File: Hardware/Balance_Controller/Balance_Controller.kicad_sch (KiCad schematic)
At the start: 101 parts, among them J1 COM_SW, J10 VESC-, J11 SWD, J12 BLE PROG, J13 RGB_LED, J14 ENABLE, J15 CAN, J2 CHRG_SW, J3 LOAD_SW, J4 BATT+, J5 BATT-, J6 BAL_BATT, J7 BAL_CHRG, J8 CHARGE, J9 VESC+, SW1 NRST, SW2 BOOT0, T1 TestPoint, T10 TestPoint, T11 TestPoint, T2 TestPoint, T3 TestPoint, T4 TestPoint, T6 TestPoint, T7 TestPoint, U1 MPM3610GQV-P, U2 MPM3610GQV-P, U3 TPS2116DRLR, U4 MCP111T-195I/LB, U5 STM32F412CGU6, U6 RN4871-I/RM140, U7 TJA1051TK-3, U8 MPU-6050, Y1 NX3225SA-16.000

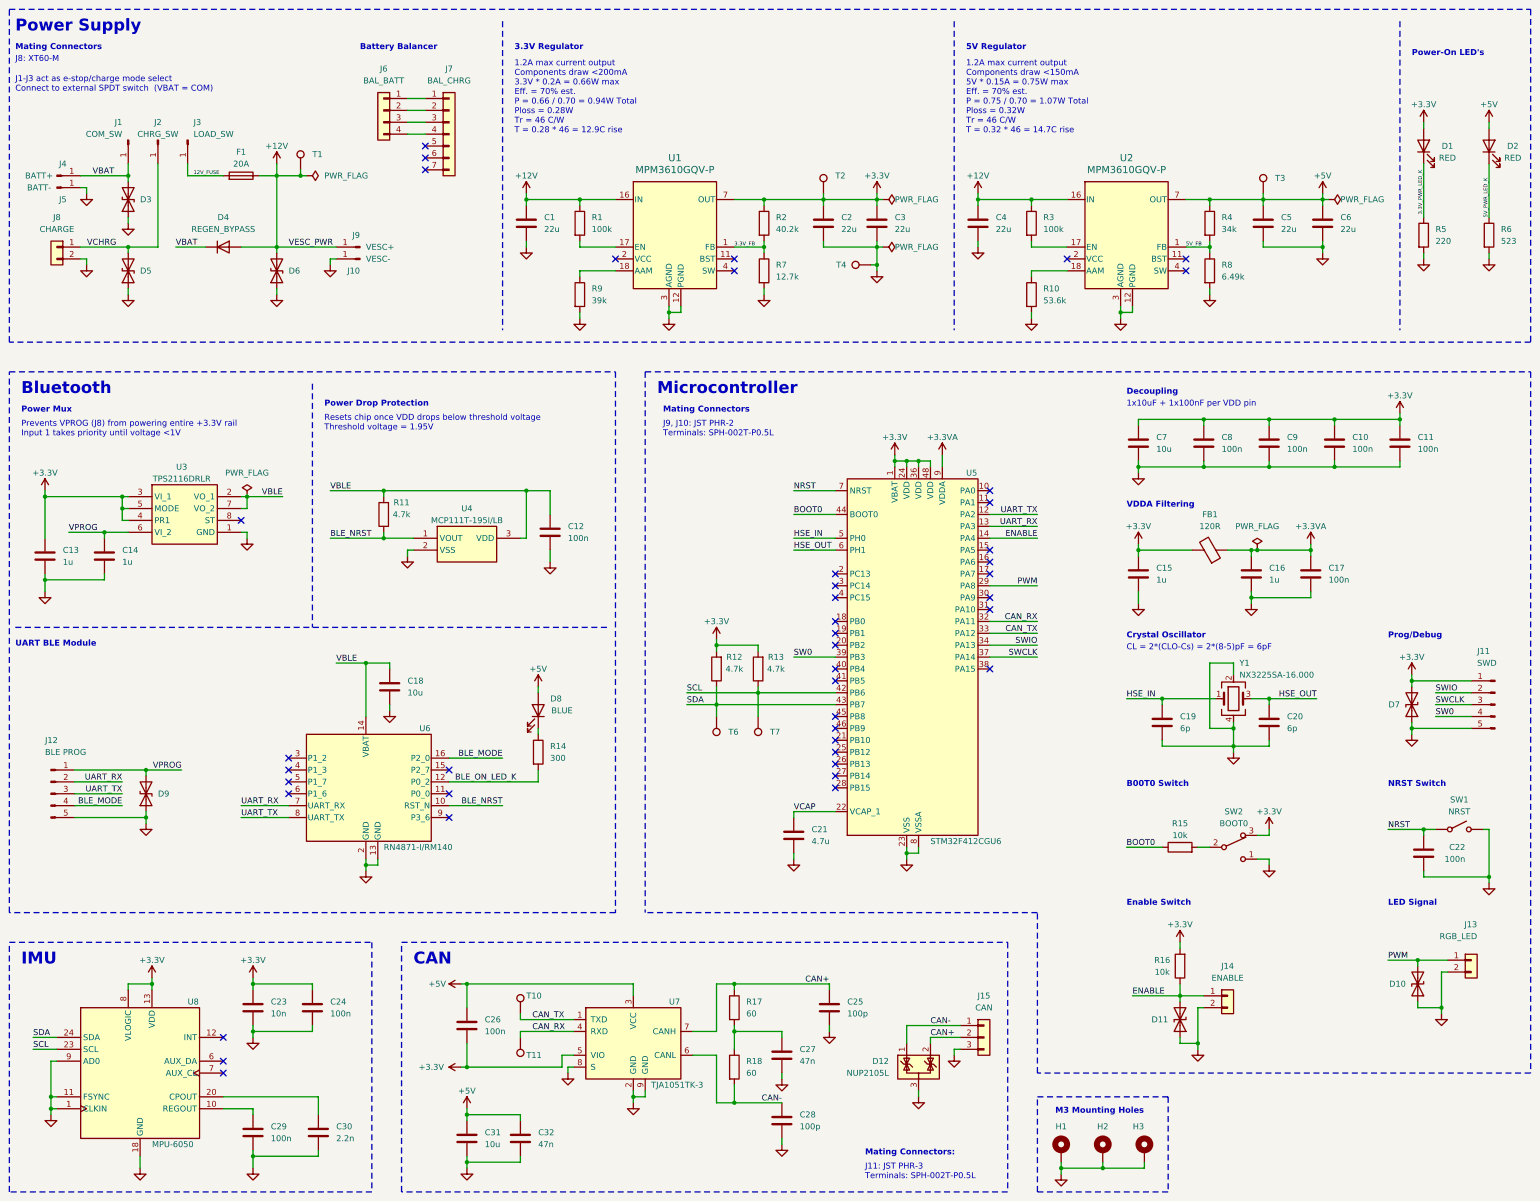
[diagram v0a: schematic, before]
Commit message: Updated schematic and routing
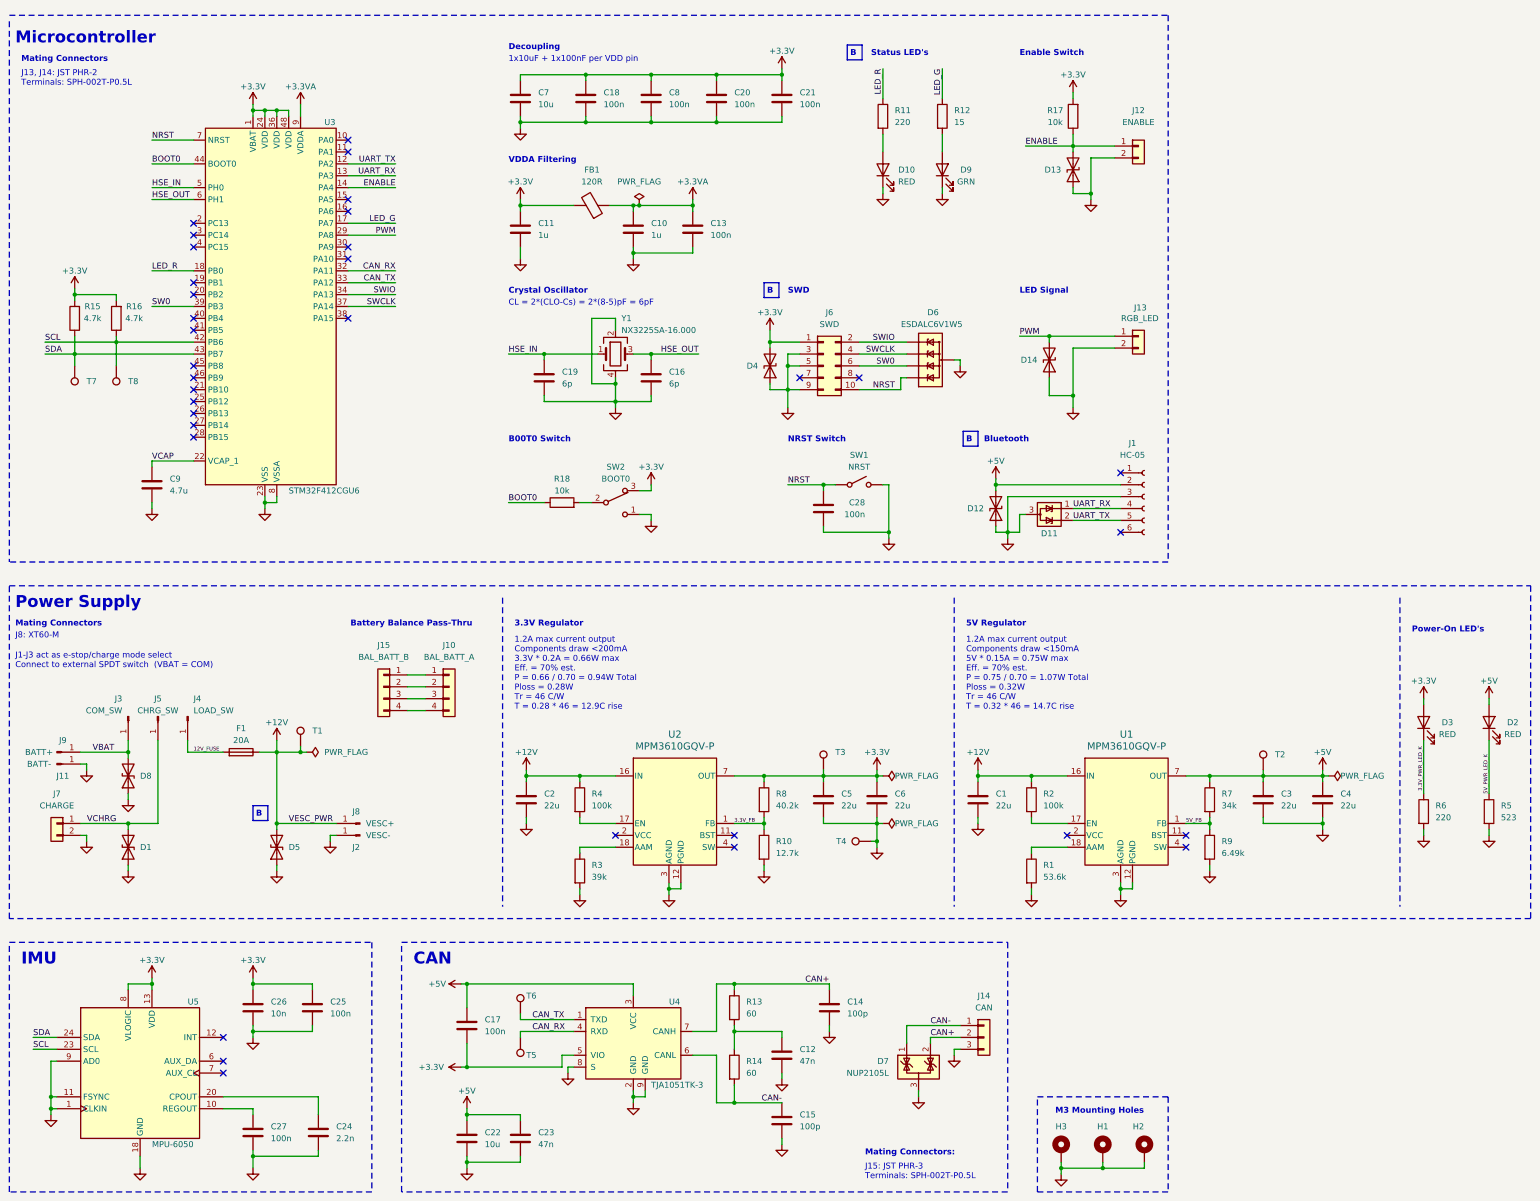
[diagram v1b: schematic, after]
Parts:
- removed C12: 100n, Capacitor_SMD:C_0603_1608Metric, symbol Device:C
- removed C13, C14: 1u, Capacitor_SMD:C_0805_2012Metric, symbol Device:C
- removed C18: 10u, Capacitor_SMD:C_1206_3216Metric, symbol Device:C
- removed D4: REGEN_BYPASS, SBM3060VDC-AU_R2_006A1:SBM3060VDCAU_R2_006A1, symbol SBM3060VDC-AU_R2_006A1:SBM3060VDC-AU_R2_006A1
- removed D7, D9: SC1533-01FTG, Diode_SMD:D_SOD-323, symbol Device:D_TVS
- removed D8: BLUE, LED_SMD:LED_0805_2012Metric, symbol Device:LED
- removed J11: SWD, Connector_PinHeader_1.27mm:PinHeader_1x05_P1.27mm_Vertical, symbol Connector:Conn_01x05_Pin
- removed J12: BLE PROG, Connector_PinHeader_1.27mm:PinHeader_1x05_P1.27mm_Vertical, symbol Connector:Conn_01x05_Pin
- removed J7: BAL_CHRG, Connector_JST:JST_XH_B7B-XH-A_1x07_P2.50mm_Vertical, symbol Connector_Generic:Conn_01x07
- removed R14: 300, Resistor_SMD:R_0603_1608Metric, symbol Device:R
- removed U3: TPS2116DRLR, TPS2116DRLR:SOTFL50P160X60-8N, symbol TPS2116DRLR:TPS2116DRLR
- removed U4: MCP111T-195I/LB, MCP111T-195I/LB:SOT65P210X110-3N, symbol MCP111T-195I_LB:MCP111T-195I_LB
- removed U6: RN4871-I/RM140, RN4871-I/RM140:RN4871_MCH, symbol RN4871-I/RM140:RN4871-I_RM140
- added D10: RED, LED_SMD:LED_0805_2012Metric, symbol Device:LED
- added D11: VESD03A2-03G-G3-08, Package_TO_SOT_SMD:SOT-323_SC-70, symbol VESD: VESD03A2-03G-G3-08
- added D12, D4: SC1533-01FTG, Diode_SMD:D_SOD-323, symbol Device:D_TVS
- added D6: ESDALC6V1W5, ESDALC6V1W5:SOT65P210X110-5N, symbol ESDALC6V1W5:ESDALC6V1W5
- added D9: GRN, LED_SMD:LED_0805_2012Metric, symbol Device:LED
- added J1: HC-05, Connector_PinSocket_2.54mm:PinSocket_1x06_P2.54mm_Vertical, symbol Connector:Conn_01x06_Socket
- added J10: BAL_BATT_A, Connector_JST:JST_XH_B4B-XH-A_1x04_P2.50mm_Vertical, symbol Connector_Generic:Conn_01x04
- added J6: SWD, Connector_PinHeader_1.27mm:PinHeader_2x05_P1.27mm_Vertical_SMD, symbol Connector_Generic:Conn_02x05_Odd_Even
- added R12: 15, Resistor_SMD:R_0603_1608Metric, symbol Device:R
- J15: renamed from J6; value BAL_BATT -> BAL_BATT_B
- R11: value 4.7k -> 220; PN MCT0603MD4701BP500 -> ERJ-UP3J221V
- T1: footprint RCU-0C:TP+195X110 -> RCT-0C:RCT-0C; MPN RCU-0C -> RCT-0C
- T2: renamed from T3; footprint RCU-0C:TP+195X110 -> RCT-0C:RCT-0C; PN RCU-0C -> RCT-0C
- T3: renamed from T2; footprint RCU-0C:TP+195X110 -> RCT-0C:RCT-0C; PN RCU-0C -> RCT-0C
- T4: footprint RCU-0C:TP+195X110 -> RCT-0C:RCT-0C
- U3: renamed from U5; footprint Package_DFN_QFN:QFN-48-1EP_7x7mm_P0.5mm_EP5.6x5.6mm -> STM32F412:QFN-48-1EP_7x7mm_P0.5mm_EP5.6x5.6mm
- U5: renamed from U8; footprint Sensor_Motion:InvenSense_QFN-24_4x4mm_P0.5mm -> MPU6050:InvenSense_QFN-24_4x4mm_P0.5mm
- renumbered C4 to C1, C16 to C10, C15 to C11, C27 to C12, C17 to C13, C25 to C14, C28 to C15, C20 to C16, C26 to C17, C8 to C18, C1 to C2, C10 to C20, C11 to C21, C31 to C22, C32 to C23, C30 to C24, C24 to C25, C23 to C26, C29 to C27, C22 to C28, C5 to C3, C6 to C4, C2 to C5, C3 to C6, C9 to C8, C21 to C9, D5 to D1, D11 to D13, D10 to D14, D1 to D3, D6 to D5, D12 to D7, D3 to D8, H2 to H1, H3 to H2, H1 to H3, J5 to J11, J14 to J12, J15 to J14, J10 to J2, J1 to J3, J3 to J4, J2 to J5, J8 to J7, J9 to J8, J4 to J9, R10 to R1, R7 to R10, R17 to R13, R18 to R14, R12 to R15, R13 to R16, R16 to R17, R15 to R18, R3 to R2, R9 to R3, R1 to R4, R6 to R5, R5 to R6, R4 to R7, R2 to R8, R8 to R9, T11 to T5, T10 to T6, T6 to T7, T7 to T8, U2 to U1, U1 to U2, U7 to U4
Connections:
- net BLE_NRST is gone; now on net LED_R: R11.1
- net +3.3V: now also D4.2 (A2), J6.1 (Pin_1)
- net +5V: now also D12.2 (A2), J1.2 (Pin_2)
- net GND: now also D10.1 (K), D11.3 (GND), D12.1 (A1), D4.1 (A1), D6.2 (GND), D9.1 (K), J1.3 (Pin_3), J6.3 (Pin_3), J6.5 (Pin_5), J6.9 (Pin_9)
- net NRST: now also D6.1 (IO1), J6.10 (Pin_10)
- net SW0: now also D6.5 (IO4), J6.6 (Pin_6)
- net SWCLK: now also D6.4 (IO3), J6.4 (Pin_4)
- net SWIO: now also D6.3 (IO2), J6.2 (Pin_2)
- net UART_RX: now also D11.1 (IO1), J1.4 (Pin_4)
- net UART_TX: now also D11.2 (IO2), J1.5 (Pin_5)
- net LED_G: now reaches U3.17 (PA7)
- net LED_G: now also R12.1
- net LED_R: now reaches U3.18 (PB0)
- net at J15.1 (Pin_1): now also J10.1 (Pin_1)
- net at J15.2 (Pin_2): now also J10.2 (Pin_2)
- net at J15.3 (Pin_3): now also J10.3 (Pin_3)
- net at J15.4 (Pin_4): now also J10.4 (Pin_4)
- net VBLE: no longer names the net of R11.2
- net VBLE: now also D10.2 (A)
- new net: D9.2 (A), R12.2
- no-connect marks 43 -> 34
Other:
- note added: "B"
- note added: "Battery Balance Pass-Thru"
- note added: "J13, J14: JST PHR-2 Terminals: SPH-002T-P0.5L"
- note added: "J15: JST PHR-3 Terminals: SPH-002T-P0.5L"
- note added: "SWD"
- note added: "Status LED's"
- note removed: "Battery Balancer"
- note removed: "J11: JST PHR-3 Terminals: SPH-002T-P0.5L"
- note removed: "J9, J10: JST PHR-2 Terminals: SPH-002T-P0.5L"
- note removed: "Power Drop Protection"
- note removed: "Power Mux"
- note removed: "Prevents VPROG (J8) from powering entire +3.3V rail Input 1 takes priority until voltage <1V"
- note removed: "Prog/Debug"
- note removed: "Resets chip once VDD drops below threshold voltage Threshold voltage = 1.95V"
- note removed: "UART BLE Module"
- company: Created By: Austyn Loehr -> (none)
- title: Reaction Wheel Controller -> Balance Controller
- moved on the sheet: C1, C10, C11, C13, C16, C18, C19, C2, C20, C21, C28, C3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

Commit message: Created updated BOM and manufacturing files
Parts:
- C1, C2, C3, C4, C5, C6: MFG (none) -> Murata; MPN (none) -> GRM32ER71E226KE15L; PN GRM32ER71E226KE15L -> (none)
- C10, C11: MFG (none) -> Murata; MPN (none) -> GRM21BR71C105KA01K; PN GRM21BR71C105KA01K -> (none)
- C12, C23: MFG (none) -> Murata; MPN (none) -> GCJ188R71C473KA01D; PN GCJ188R71C473KA01D -> (none)
- C13, C17, C18, C20, C21, C25, C27, C28, C8: MFG (none) -> Murata; MPN (none) -> GRM188R72A104KA35J; PN GRM188R72A104KA35J -> (none)
- C14, C15: MFG (none) -> Murata; MPN (none) -> GCM1885C1H101JA16J; PN GCM1885C1H101JA16J -> (none)
- C16, C19: MFG (none) -> Murata; MPN (none) -> GRM1885C2A6R0DA01D; PN GRM1885C2A6R0DA01D -> (none)
- C22, C7: MFG (none) -> Murata; MPN (none) -> GRM31CR71E106MA12L; PN GRM31CR71E106MA12L -> (none)
- C24: MFG (none) -> Murata; MPN (none) -> GRT1885C1H222JA02D; PN GRT1885C1H222JA02D -> (none)
- C26: MFG (none) -> Murata; MPN (none) -> GRM1885C1H103JA01J; PN GRM1885C1H103JA01J -> (none)
- C9: MFG (none) -> Murata; MPN (none) -> GRM21BZ71E475KE15L; PN GRM21BZ71E475KE15L -> (none)
- D1, D5: MFG (none) -> Panjit; Manufacturer Panjit -> (none)
- D10, D2, D3: MFG (none) -> Wurth Elektronik; MPN (none) -> 150080SS75000; PN 150080SS75000 -> (none)
- D11: MFG (none) -> Vishay; MPN (none) -> VESD03A2-03G-G3-08; Manufacturer_Part_Number 78-VESD03A2-03G-G308 -> (none); Mouser Part Number VESD03A2-03G-G3-08 -> (none)
- D12, D13, D14, D4: MFG (none) -> Littelfuse; MPN (none) -> SC1533-01FTG; PN SC1533-01FTG -> (none)
- D6: MFG (none) -> ST; MPN (none) -> ESDALC6V1W5; Manufacturer_Name STMicroelectronics -> (none); Manufacturer_Part_Number ESDALC6V1W5 -> (none)
- D7: MFG (none) -> Diotec; MPN (none) -> NUP2105L
- D8: MFG (none) -> Panjit; Manufactuer Panjit -> (none)
- D9: MFG (none) -> Wurth Elektronik; Manufacturer Wurth Elektronik -> (none)
- F1: MFG (none) -> Keystone Electronics; Manufacturer_Name Keystone Electronics -> (none); Manufacturer_Part_Number 3568 -> (none)
- FB1: MFG (none) -> Murata; MPN (none) -> BLM18KG121TN1D; PN BLM18KG121TN1D -> (none)
- H1, H2, H3, J11, J2, J3, J4, J5, J8, J9: now left out of the parts list
- J1: MFG (none) -> Wurth Elektronik; MPN (none) -> 61300611821
- J10, J15: MFG (none) -> JST; Manufacturer JST -> (none)
- J12, J13: MFG (none) -> JST; MPN (none) -> B2B-PH-K; PN B2B-PH-K -> (none)
- J14: MFG (none) -> JST; MPN (none) -> B3B-PH-K; PN B3B-PH-K -> (none)
- J6: MFG (none) -> Samtec; Manufacturer Samtec -> (none)
- J7: MFG (none) -> AMASS; Manufacturer AMASS -> (none)
- R1: MFG (none) -> Panasonic; MPN (none) -> ERJ-PA3F5362V; PN ERJ-PA3F5362V -> (none)
- R10: MFG (none) -> Vishay; MPN (none) -> CRCW060312K7FKEAHP; PN CRCW060312K7FKEAHP -> (none)
- R11, R6: MFG (none) -> Panasonic; MPN (none) -> ERJ-UP3J221V; PN ERJ-UP3J221V -> (none)
- R12: MFG (none) -> Panasonic; MPN (none) -> ERJ-UP3F15R0V; Manufacturer Panasonic -> (none); PN ERJ-UP3F15R0V -> (none)
- R13, R14: MFG (none) -> Panasonic; MPN (none) -> ERJ-UP3F60R4V; PN ERJ-UP3F60R4V -> (none)
- R15, R16: MFG (none) -> Vishay; MPN (none) -> MCT0603MD4701BP500; PN MCT0603MD4701BP500 -> (none)
- R17, R18: MFG (none) -> ROHM; MPN (none) -> ESR03EZPJ103; PN ESR03EZPJ103 -> (none)
- R2, R4: MFG (none) -> Panasonic; MPN (none) -> ERJ-UP3F1003V; PN ERJ-UP3F1003V -> (none)
- R3: MFG (none) -> Panasonic; MPN (none) -> ERJ-UP3J393V; PN ERJ-UP3J393V -> (none)
- R5: MFG (none) -> Panasonic; MPN (none) -> ERJ-PA3F5230V; PN ERJ-PA3F5230V -> (none)
- R7: MFG (none) -> Panasonic; MPN (none) -> ERJ-PB3D3402V; PN ERJ-PB3D3402V -> (none)
- R8: MFG (none) -> Vishay; MPN (none) -> RCS060340K2FKEA; PN RCS060340K2FKEA -> (none)
- R9: MFG (none) -> Panasonic; MPN (none) -> ERJ-PA3F6491V; PN ERJ-PA3F6491V -> (none)
- SW1: MFG (none) -> C&K; MPN (none) -> PTS815 SJG 250 SMTR LFS; Manufacturer_Name C & K COMPONENTS -> (none); Manufacturer_Part_Number PTS815 SJG 250 SMTR LFS -> (none)
- SW2: MFG (none) -> C&K; MPN (none) -> AYZ0102AURLC; PN AYZ0102AURLC -> (none)
- T1: MFG (none) -> TE; Manufacturer TE Connectivity -> (none)
- T2, T3: MFG (none) -> TE; MPN (none) -> RCT-0C; PN RCT-0C -> (none)
- T4, T5, T6, T7, T8: MFG (none) -> TE; MPN (none) -> RCU-0C; PN RCU-0C -> (none)
- U1, U2: MFG (none) -> Monolithic Power Systems
- U3: MFG (none) -> ST; MPN (none) -> STM32F412CGU6
- U4: MFG (none) -> NXP; MPN (none) -> TJA1051TK/3,118
- U5: MFG (none) -> TDK InvenSense
- Y1: MFG (none) -> NDK; MPN (none) -> NX3225SA-16.000M-STD-CRS-2; Part Number NX3225SA-16.000M-STD-CRS-2 -> (none)
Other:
- note added: "J12, J13: JST PHR-2 Terminals: SPH-002T-P0.5L"
- note added: "J14: JST PHR-3 Terminals: SPH-002T-P0.5L"
- note added: "J3-J5 act as e-stop/charge mode select Connect to external SPDT switch (VBAT = COM)"
- note added: "J7: XT60-M"
- note removed: "J1-J3 act as e-stop/charge mode select Connect to external SPDT switch (VBAT = COM)"
- note removed: "J13, J14: JST PHR-2 Terminals: SPH-002T-P0.5L"
- note removed: "J15: JST PHR-3 Terminals: SPH-002T-P0.5L"
- note removed: "J8: XT60-M"

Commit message: Updated XT60 PN and added render
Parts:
- J7: MPN XT60-F -> XT60PB-F
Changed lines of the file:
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@@
 			)
 		)
-		(property "MPN" "XT60-F"
+		(property "MPN" "XT60PB-F"
 			(at 57.15 194.31 0)
 			(effects
